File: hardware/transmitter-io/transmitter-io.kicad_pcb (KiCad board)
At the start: 2 copper layers, 60 x 60 mm, 22 parts, among them J1 IO EXTENSION, J2 DIMMER_B, J5 12V_A, J6 12V_B, U1 LM317T, U2 74LS164, U3 TLC7226A, U4 LM324A

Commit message: Add analog, pwm, dmx, and io boards. Still needs work.
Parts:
- removed C1, C2, C3, C4: .01uF, Capacitors:CAP-PTH-2.54
- removed C5: 10uF, Capacitor_THT:CP_Radial_D5.0mm_P2.50mm
- removed J2: DIMMER_B, Connector_Phoenix_MSTB:PhoenixContact_MSTBA_2,5_5-G-5,08_1x05_P5.08mm_Horizontal
- removed J5: 12V_A, Connector_BarrelJack:BarrelJack_CUI_PJ-063AH_Horizontal
- removed J6: 12V_B, Connector_Phoenix_MSTB:PhoenixContact_MSTBA_2,5_2-G-5,08_1x02_P5.08mm_Horizontal
- removed MH1, MH2, MH3, MH4: MountingHole, MountingHole:MountingHole_3.2mm_M3
- removed U1: LM317T, Package_TO_SOT_THT:TO-220-3_Horizontal_TabDown
- removed U2: 74LS164, Package_DIP:DIP-14_W7.62mm
- removed U3: TLC7226A, Package_DIP:DIP-20_W7.62mm
- removed U4: LM324A, Package_DIP:DIP-14_W7.62mm
- added A1: Arduino_UNO_R3, footprints:ARDUINO_R3_NO_HOLES, F.Cu at (150.6, 89.9)
- added D1: DATA, LED_THT:LED_D5.0mm, F.Cu at (182.2, 96.5)
- added D2: CLOCK, LED_THT:LED_D5.0mm, F.Cu at (182.2, 83.7)
- added D3: DIM3, LED_THT:LED_D5.0mm, F.Cu at (175.1, 71.1)
- added D4: DIM2, LED_THT:LED_D5.0mm, F.Cu at (168.3, 71.1)
- added D5: DIM1, LED_THT:LED_D5.0mm, F.Cu at (161.4, 71.1)
- added D6: DIM0, LED_THT:LED_D5.0mm, F.Cu at (154.6, 71.1)
- added D7: CLK_FST, LED_THT:LED_D5.0mm, F.Cu at (164.2, 92.3)
- added R1: 330, Resistor_THT:R_Axial_DIN0207_L6.3mm_D2.5mm_P10.16mm_Horizontal, F.Cu at (176.0, 88.1)
- added R2: 330, Resistor_THT:R_Axial_DIN0207_L6.3mm_D2.5mm_P10.16mm_Horizontal, F.Cu at (172.7, 88.1)
- added R3: 330, Resistor_THT:R_Axial_DIN0207_L6.3mm_D2.5mm_P10.16mm_Horizontal, F.Cu at (166.2, 78.5)
- added R4: 330, Resistor_THT:R_Axial_DIN0207_L6.3mm_D2.5mm_P10.16mm_Horizontal, F.Cu at (166.2, 81.7)
- added R5: 330, Resistor_THT:R_Axial_DIN0207_L6.3mm_D2.5mm_P10.16mm_Horizontal, F.Cu at (166.2, 84.8)
- added R6: 330, Resistor_THT:R_Axial_DIN0207_L6.3mm_D2.5mm_P10.16mm_Horizontal, F.Cu at (163.8, 78.5)
- added S1: DIM_SELECT, Switches:TACTILE_SWITCH_PTH_12MM, F.Cu at (143.4, 74.3)
- added S2: CLOCK_MODE, Switches:TACTILE_SWITCH_PTH_12MM, F.Cu at (159.3, 104.0)
- added S3: CLOCK_STEP, Switches:TACTILE_SWITCH_PTH_12MM, F.Cu at (143.4, 104.0)
- added VR1: 10k, Resistors:SLIDER-SMALL, F.Cu at (124.8, 86.1)
- added VR2: 10k, Resistors:POT-PTH-ALPS, F.Cu at (143.4, 89.1)
- D8: value 1N5819 -> CLK_SLO; footprint Diode_THT:D_DO-41_SOD81_P10.16mm_Horizontal -> LED_THT:LED_D5.0mm
- J1: value IO EXTENSION -> Output; footprint Connector_IDC:IDC-Header_2x07_P2.54mm_Horizontal -> Connector_PinHeader_2.54mm:PinHeader_1x03_P2.54mm_Horizontal
- R7: value 390 -> 330
- R8: value 2.7k -> 330
- moved R7 52.2 mm to (163.8, 81.7), turned to 180 degrees
- moved R8 43.9 mm to (163.8, 84.8)
- moved D8 24.2 mm to (157.1, 92.3)
- moved J1 21.5 mm to (173.5, 103.9), turned to 0 degrees
- moved G*** 15.5 mm to (120.1, 109.5)
- moved ? 8.50 mm to (119.1, 114.3)
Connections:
- D8 pad 1: Net-(D8-Pad1) -> /~CLK_SLO
- J1 pad 1: +5V -> /RXCLK
- J1 pad 2: +5V -> GND
- J1 pad 3: /~WR -> /RX
- R7 pad 1: Net-(R7-Pad1) -> +5V
- R7 pad 2: +10V -> Net-(D7-Pad2)
- R8 pad 1: GND -> +5V
- R8 pad 2: Net-(R7-Pad1) -> Net-(D8-Pad2)
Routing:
- net /A4: track 0.00 -> 72.4 mm
- net /A1: track 0.00 -> 68.7 mm
- net /RX: track 0.00 -> 65.7 mm
- net /RXCLK: track 0.00 -> 59.4 mm
- net /A0: track 0.00 -> 50.1 mm
- net /A5: track 0.00 -> 46.0 mm
- net /~DATA: track 0.00 -> 36.6 mm
- net /~CLK_FST: track 0.00 -> 35.2 mm
- net /~CLK_SLO: track 0.00 -> 30.6 mm
- net /~CLOCK: track 0.00 -> 24.7 mm
- net Net-(D5-Pad2): track 0.00 -> 22.9 mm
- net /A2: track 0.00 -> 18.6 mm
- net Net-(D2-Pad2): track 0.00 -> 18.2 mm
- net Net-(D7-Pad2): track 0.00 -> 15.0 mm
- net Net-(D4-Pad2): track 0.00 -> 13.3 mm
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- removed copper zone on F.Cu, net +10V
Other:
- board size 60 x 60 mm -> 68.6 x 53.3 mm
- net class Power added: clearance 0.1524, trace_width 0.3048, via_dia 1.27, via_drill 0.635
- board text added: "Clock"
- board text added: "Clock Mode"
- board text added: "Clock Speed"
- board text added: "Clock Step"
- board text added: "D G C"
- board text added: "DMX-TX1"
- board text added: "DMX-TX1, Rev 1.2 Crazy Giraffe Software"
- board text added: "Data"
- board text added: "Dim Select"
- board text added: "Dim1"
- board text added: "Dim2"
- board text added: "Dim3"
- board text added: "Dim4"
- board text added: "Dimmer Level"
- board text added: "Fast"
- board text added: "Output"
- board text added: "Slow"
- board text removed: "- +"
- board text removed: "12v In"
- board text removed: "DMX-DA1"
- board text removed: "DMX-DA1, Rev 1.1 Crazy Giraffe Software"
- board text removed: "G 1 2 3 4 0-10v Dimmer Out"
- board text removed: "IO EXPANSION"
- board text removed: "J5/6"

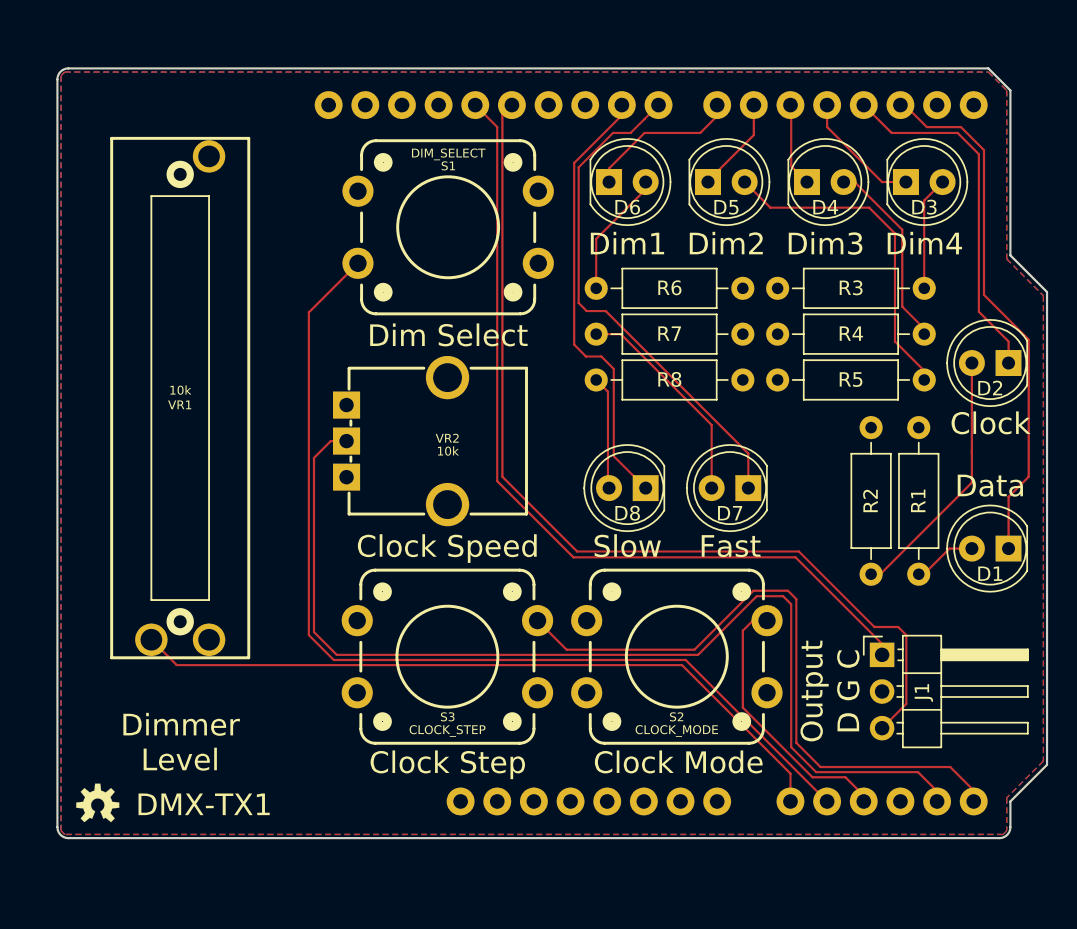
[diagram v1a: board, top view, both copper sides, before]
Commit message: Move TX2 to tx-io
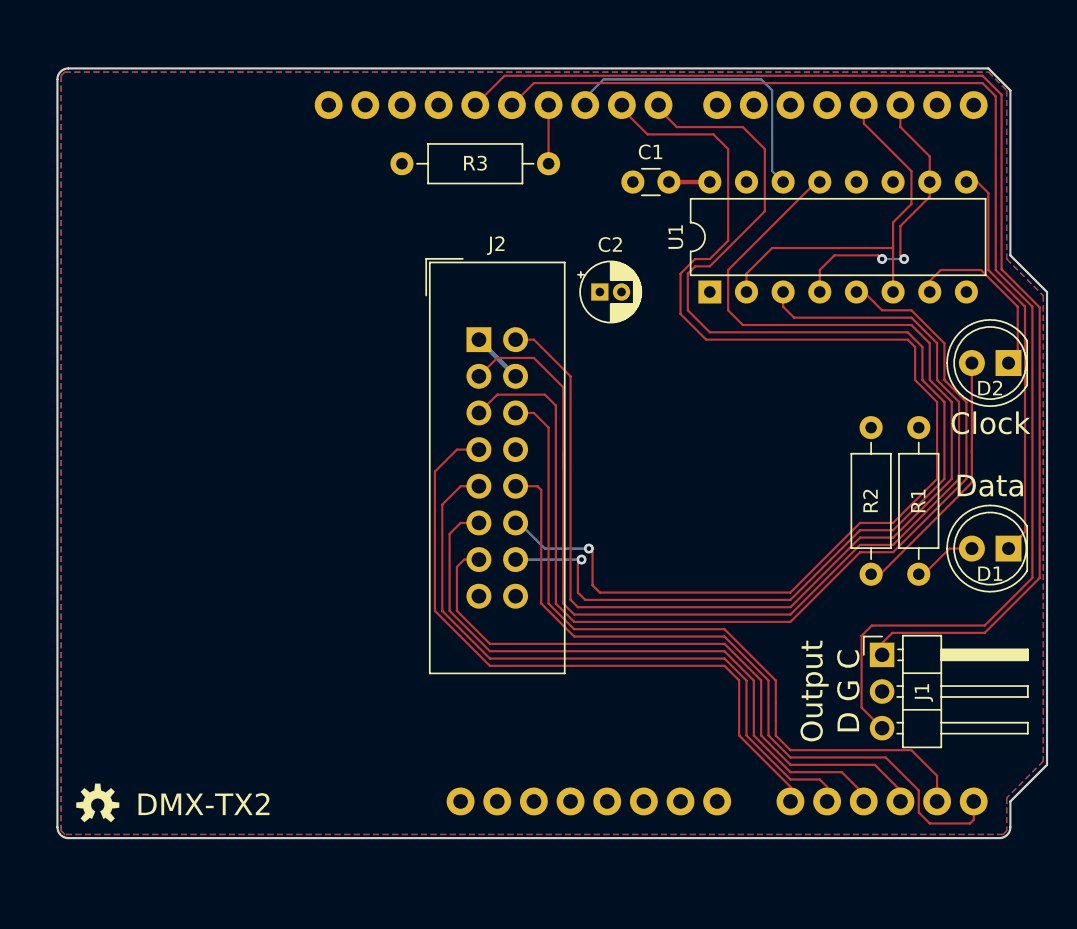
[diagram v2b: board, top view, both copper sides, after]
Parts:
- removed D3: DIM3, LED_THT:LED_D5.0mm
- removed D4: DIM2, LED_THT:LED_D5.0mm
- removed D5: DIM1, LED_THT:LED_D5.0mm
- removed D6: DIM0, LED_THT:LED_D5.0mm
- removed D7: CLK_FST, LED_THT:LED_D5.0mm
- removed D8: CLK_SLO, LED_THT:LED_D5.0mm
- removed R4, R5, R6, R7, R8: 330, Resistor_THT:R_Axial_DIN0207_L6.3mm_D2.5mm_P10.16mm_Horizontal
- removed S1: DIM_SELECT, Switches:TACTILE_SWITCH_PTH_12MM
- removed S2: CLOCK_MODE, Switches:TACTILE_SWITCH_PTH_12MM
- removed S3: CLOCK_STEP, Switches:TACTILE_SWITCH_PTH_12MM
- removed VR1: 10k, Resistors:SLIDER-SMALL
- removed VR2: 10k, Resistors:POT-PTH-ALPS
- added C1: 0.1uF, Capacitor_THT:C_Disc_D3.0mm_W1.6mm_P2.50mm, F.Cu at (156.2, 71.1)
- added C2: 10uF, Capacitor_THT:CP_Radial_D4.0mm_P1.50mm, F.Cu at (153.9, 78.7)
- added J2: INPUT, Connector_IDC:IDC-Header_2x08_P2.54mm_Vertical, F.Cu at (145.5, 82.0)
- added U1: 74LS365, Package_DIP:DIP-16_W7.62mm, F.Cu at (161.5, 78.7)
- moved R3 18.1 mm to (150.4, 69.8), turned to 180 degrees
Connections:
- A1 pad 12: Net-(A1-Pad12) -> /A3
- A1 pad 17: /~DATA -> /DATA
- A1 pad 18: /~CLOCK -> /CLOCK
- A1 pad 19: /~DIM3 -> Net-(A1-Pad19)
- A1 pad 20: /~DIM2 -> Net-(A1-Pad20)
- A1 pad 21: /~DIM1 -> Net-(A1-Pad21)
- A1 pad 22: /~DIM0 -> Net-(A1-Pad22)
- A1 pad 25: Net-(A1-Pad25) -> /HWD_DT
- D1 pad 1: /~DATA -> Net-(D1-Pad1)
- D2 pad 1: /~CLOCK -> Net-(D2-Pad1)
- R3 pad 1: +5V -> Net-(A1-Pad26)
- R3 pad 2: Net-(D3-Pad2) -> GND
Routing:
- net /~HWD_DT: track 0.00 -> 87.3 mm
- net /~CLK_SLO: track 30.6 -> 85.0 mm, vias 0 -> 1
- net /~CLOCK: track 24.7 -> 77.6 mm
- net /~CLK_FST: track 35.2 -> 85.9 mm, vias 0 -> 1
- net /A3: track 0.00 -> 43.7 mm
- net /~DATA: track 36.6 -> 71.3 mm
- net Net-(D1-Pad1): track 0.00 -> 28.0 mm
- net /RXCLK: track 59.4 -> 86.6 mm
- net /CLOCK: track 0.00 -> 27.0 mm
- net /A2: track 18.6 -> 44.4 mm
- net /RX: track 65.7 -> 89.5 mm
- net /A1: track 68.7 -> 45.4 mm
- net Net-(D5-Pad2): track 22.9 -> 0.00 mm
- net /A4: track 72.4 -> 50.8 mm
- net /HWD_DT: track 0.00 -> 21.0 mm
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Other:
- board text added: "DMX-TX2"
- board text added: "DMX-TX2, Rev 1.1 Crazy Giraffe Software"
- board text removed: "Clock Mode"
- board text removed: "Clock Speed"
- board text removed: "Clock Step"
- board text removed: "DMX-TX1"
- board text removed: "DMX-TX1, Rev 1.2 Crazy Giraffe Software"
- board text removed: "Dim Select"
- board text removed: "Dim1"
- board text removed: "Dim2"
- board text removed: "Dim3"
- board text removed: "Dim4"
- board text removed: "Dimmer Level"
- board text removed: "Fast"
- board text removed: "Slow"

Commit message: Prototype version of DMX, Analog, and PWM IO Modules and both TX and RX IO interfaces.
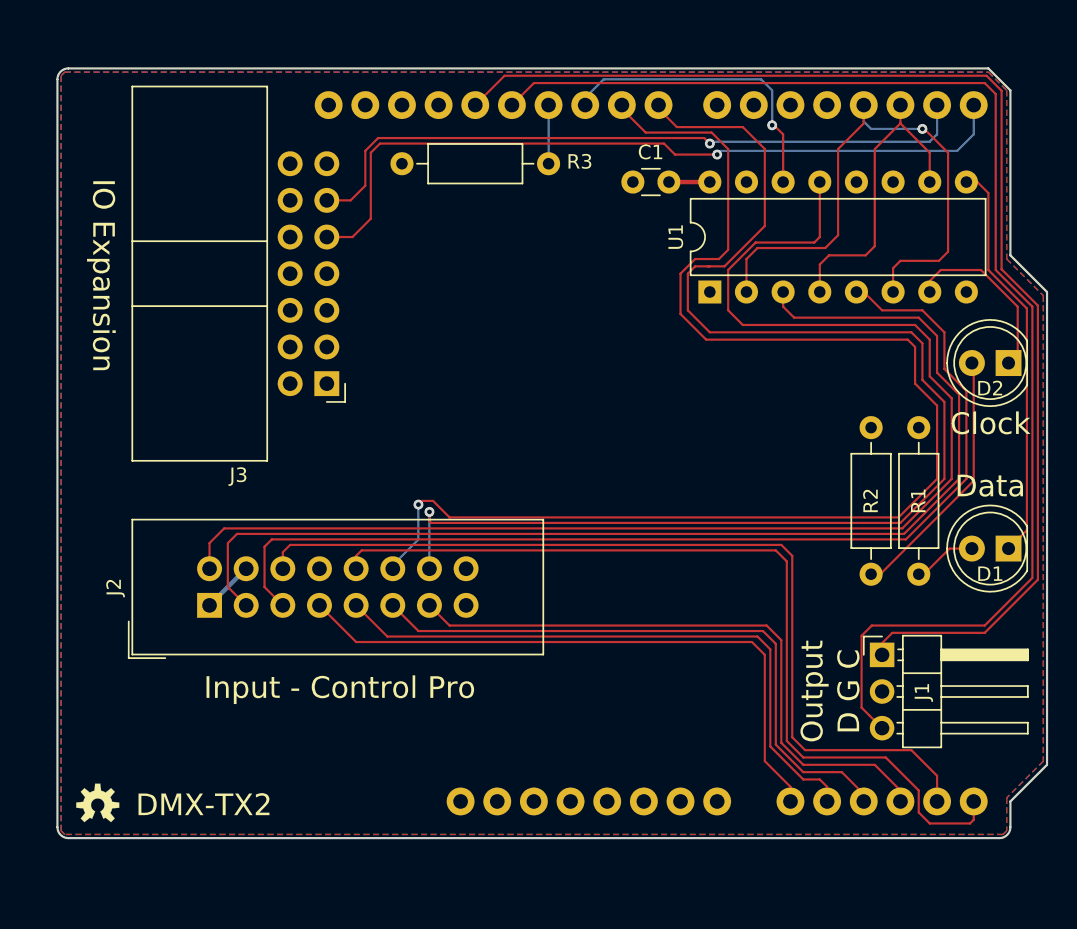
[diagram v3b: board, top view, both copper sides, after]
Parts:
- removed C2: 10uF, Capacitor_THT:CP_Radial_D4.0mm_P1.50mm
- added J3: IO EXTENSION, Connector_IDC:IDC-Header_2x07_P2.54mm_Horizontal, F.Cu at (135.0, 85.1)
- moved J2 26.2 mm to (126.9, 100.5), turned to 90 degrees
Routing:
- net Net-(A1-Pad15): track 0.00 -> 53.1 mm, vias 0 -> 1
- net Net-(A1-Pad16): track 0.00 -> 47.9 mm, vias 0 -> 1
- net /CLOCK: track 27.0 -> 39.7 mm, vias 0 -> 1
- net /A4: track 50.8 -> 62.5 mm
- net /A5: track 52.1 -> 62.8 mm
- net /~CLK_SLO: track 85.0 -> 92.3 mm
- net /~HWD_DT: track 87.3 -> 94.3 mm
- net /~CLK_FST: track 85.9 -> 92.3 mm
- net /A0: track 46.3 -> 43.2 mm
- net /~CLOCK: track 77.6 -> 80.4 mm
- net /A1: track 45.4 -> 42.8 mm
- net /~DATA: track 71.3 -> 73.2 mm
- net /A2: track 44.4 -> 42.7 mm
- net /DATA: track 20.3 -> 21.7 mm, vias 2 -> 0
- net /A3: track 43.7 -> 42.9 mm
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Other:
- board text added: "DMX-TX2, Rev 1.2 Crazy Giraffe Software"
- board text added: "IO Expansion"
- board text added: "Input - Control Pro"
- board text removed: "DMX-TX2, Rev 1.1 Crazy Giraffe Software"

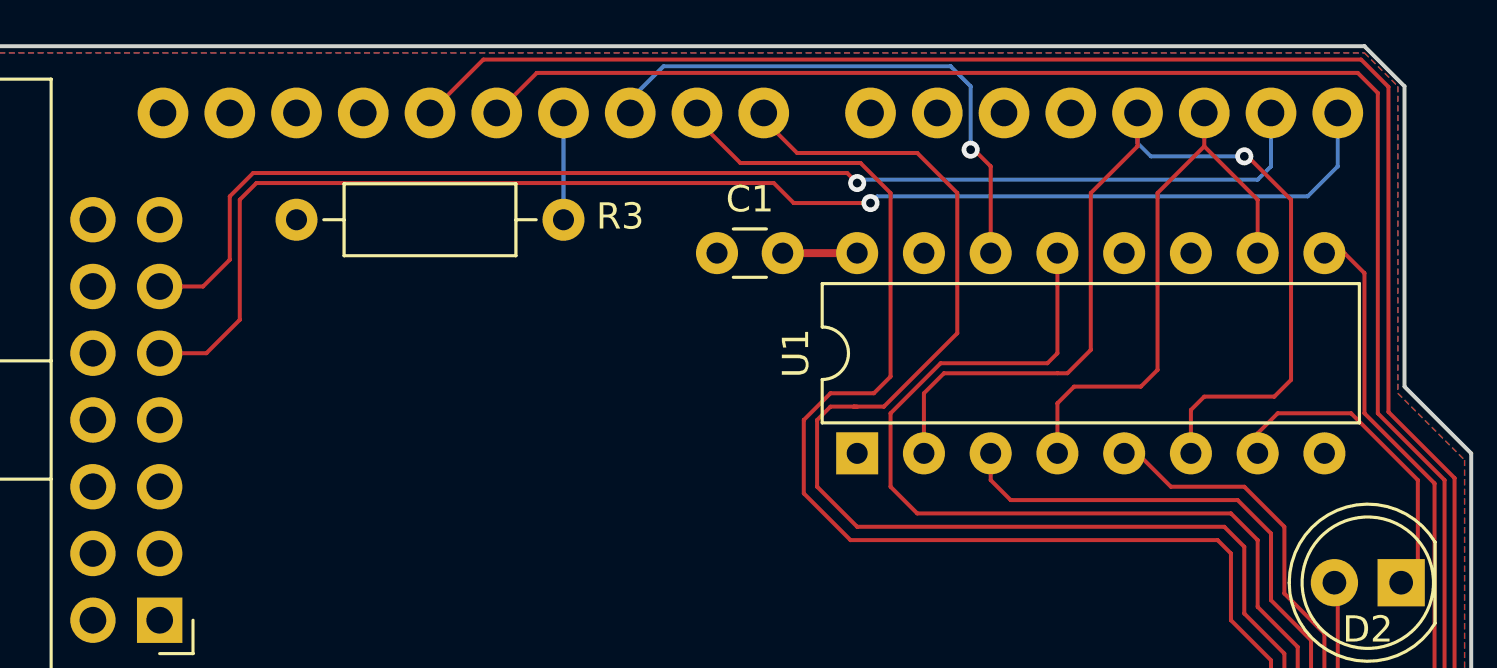
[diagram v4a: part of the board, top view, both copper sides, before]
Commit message: Ouptut local gerbers (ignored) Add detected LED to tx2
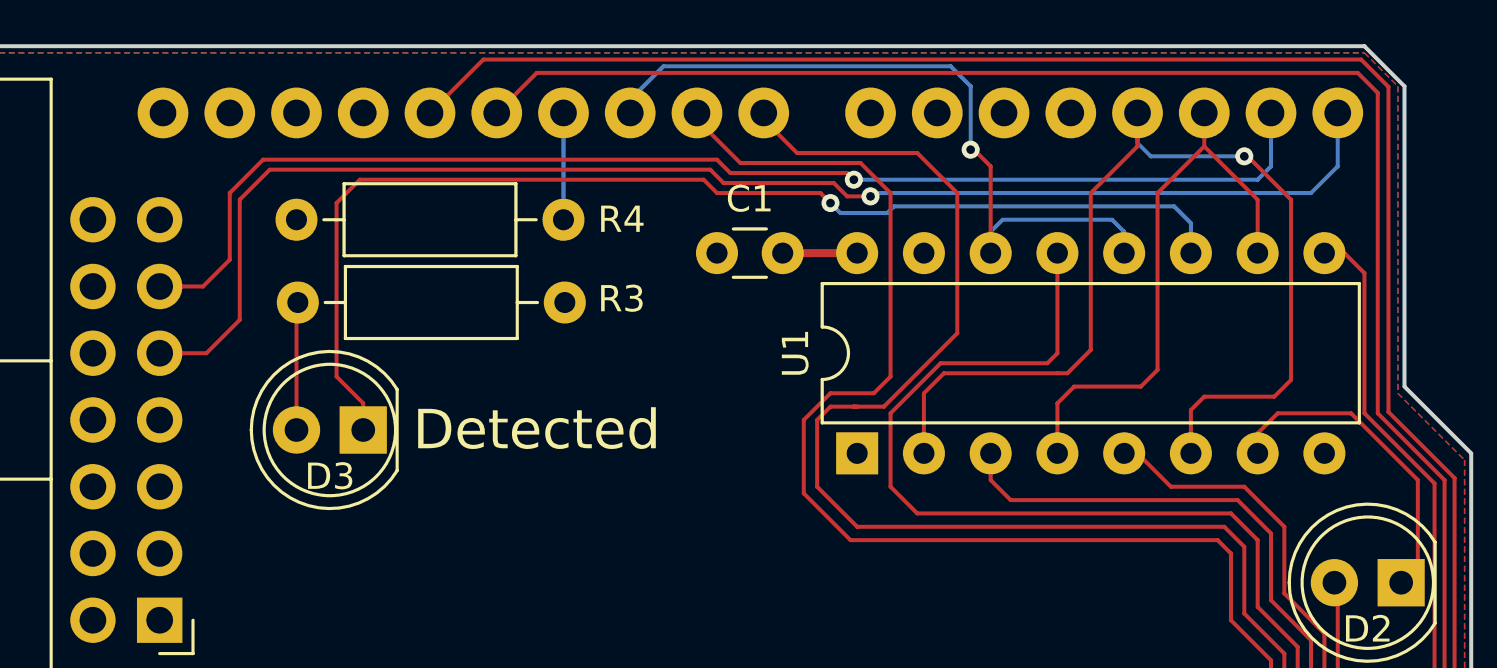
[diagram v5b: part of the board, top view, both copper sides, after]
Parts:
- added D3: DETECTED, LED_THT:LED_D5.0mm, F.Cu at (142.7, 77.9)
- added R4: 330, Resistor_THT:R_Axial_DIN0207_L6.3mm_D2.5mm_P10.16mm_Horizontal, F.Cu at (150.4, 69.8)
- moved R3 3.15 mm to (150.4, 73.0)
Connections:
- net /CLOCK renamed /~CLOCK_OUT
- net /DATA renamed /~DATA_OUT
- A1 pad 25: /HWD_DT -> /~HWD_DT_OUT
- R3 pad 1: Net-(A1-Pad26) -> +5V
- R3 pad 2: GND -> Net-(D3-Pad2)
- U1 pad 12: Net-(U1-Pad12) -> /~HWD_DT_OUT
- U1 pad 14: /HWD_DT -> /~HWD_DT_OUT
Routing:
- net Net-(D3-Pad1): track 0.00 -> 44.0 mm, vias 0 -> 1
- net /~HWD_DT_OUT: track 0.00 -> 28.1 mm, vias 0 -> 1
- net /HWD_DT: track 21.0 -> 0.00 mm, vias 1 -> 0
- net Net-(D3-Pad2): track 0.00 -> 4.87 mm
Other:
- board text added: "Detected"
